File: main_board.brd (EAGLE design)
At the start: 100.3 x 69.8 mm, 46 parts, among them P1 ST-TF-003A, U1 STM32F407VGT6, U2 USBLC6-2, U3 MCP1700T-3302E, U4 LTC4054LES5-4.2#TRPBF, X1 MicroUSB-B

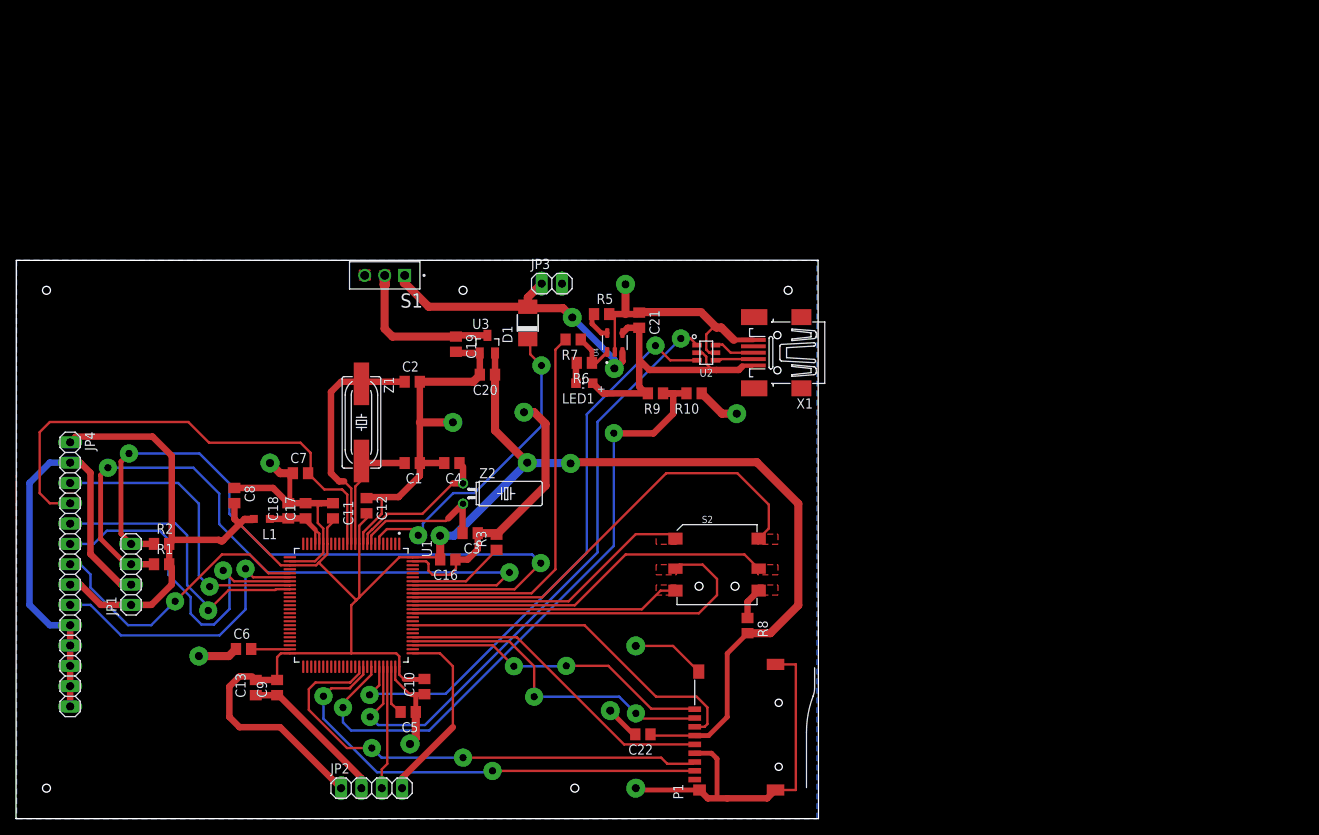
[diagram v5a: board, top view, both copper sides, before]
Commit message: updated pcb printouts
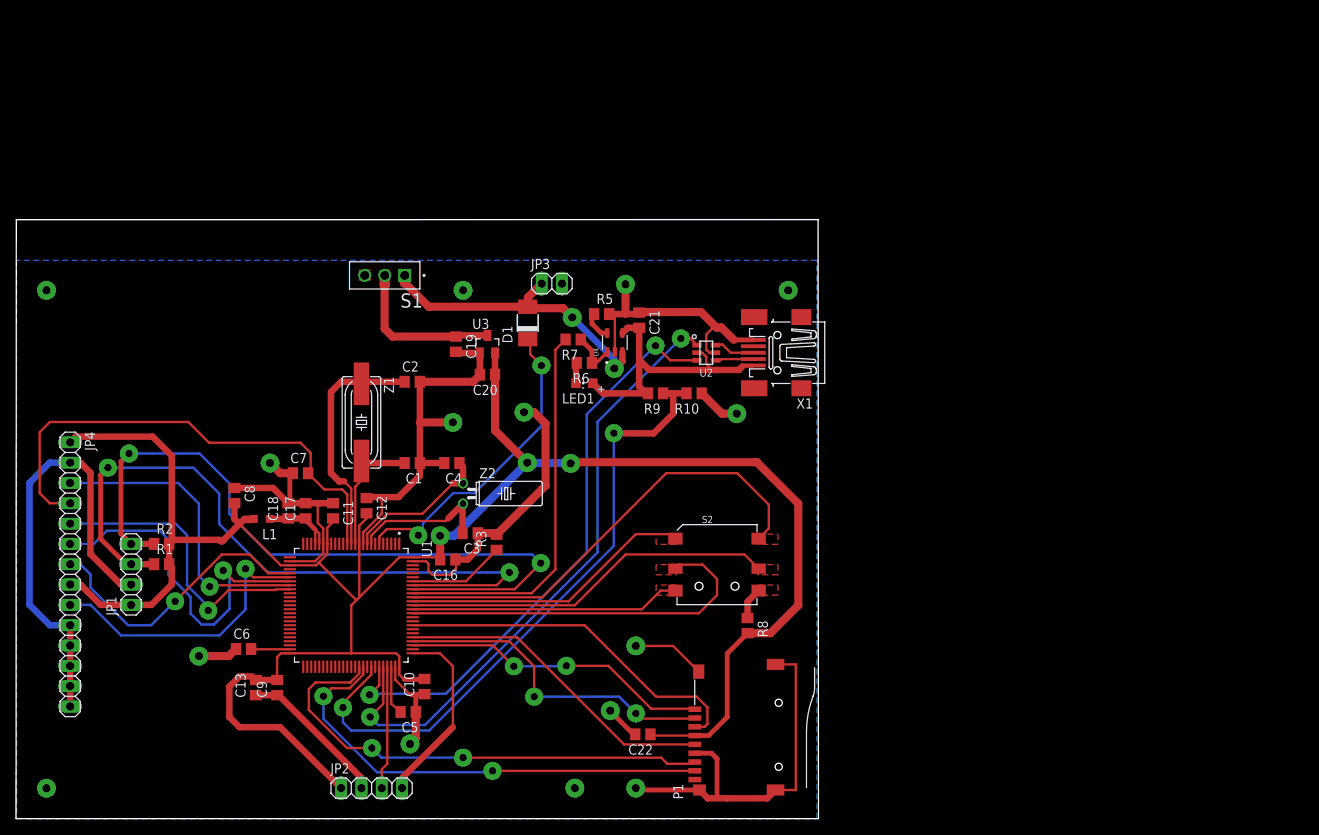
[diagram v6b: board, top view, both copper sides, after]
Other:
- board size 100.3 x 69.8 mm -> 100.3 x 74.9 mm
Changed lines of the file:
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@@
 <setting verticaltext="up"/>
 </settings>
-<grid distance="50" unitdist="mil" unit="mm" style="dots" multiple="1" display="yes" altdistance="5" altunitdist="mil" altunit="mm"/>
+<grid distance="50" unitdist="mil" unit="mm" style="dots" multiple="1" display="yes" altdistance="0.0127" altunitdist="mm" altunit="mm"/>
 <layers>
 <layer number="1" name="Top" color="4" fill="1" visible="yes" active="yes"/>
@@
 </layers>
 <board>
+<fusionsync huburn="a.YnVzaW5lc3M6cmFtYmxlcjY5Nw" projecturn="a.YnVzaW5lc3M6cmFtYmxlcjY5NyNEMjAxOTEyMjQyNDk2OTMxNTE" f3durn="urn:adsk.wipprod:dm.lineage:bHDcZ2FaTXqtTl9IB7PqNQ" pcbguid="" lastpulledtime="" lastsyncedchangeguid="" latestrevisionid="95c03de1-c068-4b4e-b2f2-ce3e2071d574" lastsyncedrevisionid="95c03de1-c068-4b4e-b2f2-ce3e2071d574" lastboardhashguid="d1d654ad-80bb-0683-6bda-78ac676d0201" lastpushedtime="2022-01-27T18:53:14Z" linktopcb3d="false"/>
 <plain>
 <wire x1="0" y1="0" x2="100.31" y2="0" width="0" layer="20" grouprefs="DISPLAY_BORDER"/>
-<wire x1="100.31" y1="0" x2="100.2592" y2="69.7994" width="0" layer="20"/>
-<wire x1="100.2592" y1="69.7994" x2="0.0381" y2="69.7867" width="0" layer="20"/>
-<wire x1="0.0381" y1="69.7867" x2="0" y2="0" width="0" layer="20" grouprefs="DISPLAY_BORDER"/>
+<wire x1="100.31" y1="0" x2="100.2592" y2="74.8794" width="0" layer="20"/>
+<wire x1="100.2592" y1="74.8794" x2="0.0381" y2="74.8667" width="0" layer="20"/>
+<wire x1="0.0381" y1="74.8667" x2="0" y2="0" width="0" layer="20" grouprefs="DISPLAY_BORDER"/>
 <wire x1="4.2291" y1="8.9408" x2="79.1591" y2="8.9408" width="0.3" layer="37" grouprefs="DISPLAY_BORDER"/>
 <wire x1="79.1591" y1="8.9408" x2="79.1591" y2="52.1208" width="0.3" layer="37" grouprefs="DISPLAY_BORDER"/>
 <wire x1="79.1591" y1="52.1208" x2="4.2291" y2="52.1208" width="0.3" layer="37" grouprefs="DISPLAY_BORDER"/>
 <wire x1="4.2291" y1="52.1208" x2="4.2291" y2="8.9408" width="0.3" layer="37" grouprefs="DISPLAY_BORDER"/>
-<hole x="3.81" y="66.04" drill="1"/>
-<hole x="3.81" y="3.81" drill="1"/>
-<hole x="96.52" y="66.04" drill="1"/>
-<hole x="69.85" y="3.81" drill="1"/>
-<hole x="55.88" y="66.04" drill="1"/>
 </plain>
 <attributes>
@@
 <contactref element="Z2" pad="1"/>
 <contactref element="C4" pad="1"/>
-<wire x1="43.91" y1="34.35" x2="43.9576" y2="34.3976" width="0.3" layer="1"/>
-<wire x1="43.9576" y1="34.3976" x2="43.9576" y2="35.59805" width="0.3" layer="1"/>
-<wire x1="43.9576" y1="35.59805" x2="44.49895" y2="36.1394" width="0.3" layer="1"/>
-<wire x1="44.51660625" y1="36.1394" x2="44.49895" y2="36.1394" width="0.3" layer="1"/>
-<wire x1="44.51660625" y1="36.1394" x2="46.47720625" y2="38.1" width="0.3" layer="1"/>
+<wire x1="43.91" y1="34.35" x2="43.9068" y2="34.3532" width="0.3" layer="1"/>
+<wire x1="43.9068" y1="35.59805" x2="43.9068" y2="34.3532" width="0.3" layer="1"/>
+<wire x1="43.9068" y1="35.59805" x2="46.40875" y2="38.1" width="0.3" layer="1"/>
 <wire x1="50.8" y1="38.1" x2="54.61" y2="41.91" width="0.3" layer="1"/>
 <wire x1="54.61" y1="41.91" x2="55.88" y2="41.91" width="0.8128" layer="1"/>
-<wire x1="46.47720625" y1="38.1" x2="50.8" y2="38.1" width="0.3" layer="1"/>
+<wire x1="46.40875" y1="38.1" x2="50.8" y2="38.1" width="0.3" layer="1"/>
 <wire x1="55.433" y1="44.45" x2="55.88" y2="44.003" width="0.3" layer="1"/>
 <wire x1="55.88" y1="44.003" x2="55.88" y2="41.91" width="0.8128" layer="1"/>
@@
 <wire x1="22.86" y1="30.353" x2="24.2062" y2="29.0068" width="0.3" layer="16"/>
 <via x="24.2062" y="29.0068" extent="1-16" drill="0.9"/>
-<wire x1="34.2154" y1="29.1719" x2="24.3713" y2="29.1719" width="0.3" layer="1"/>
+<wire x1="34.2281" y1="29.1719" x2="24.3713" y2="29.1719" width="0.3" layer="1"/>
 <wire x1="24.2062" y1="29.0068" x2="24.3713" y2="29.1719" width="0.3" layer="1"/>
-<wire x1="34.2173" y1="29.17" x2="34.2154" y2="29.1719" width="0.3" layer="1"/>
-<wire x1="34.2173" y1="29.17" x2="34.23" y2="29.17" width="0.3" layer="1"/>
+<wire x1="34.23" y1="29.17" x2="34.2281" y2="29.1719" width="0.3" layer="1"/>
 </signal>
 <signal name="LCD_DC">
@@
 <via x="24.0284" y="26.0223" extent="1-16" drill="0.9"/>
 <wire x1="24.0284" y1="26.0223" x2="26.5811" y2="28.575" width="0.3" layer="1"/>
-<wire x1="32.385" y1="28.575" x2="32.4866" y2="28.6766" width="0.3" layer="1"/>
-<wire x1="32.4866" y1="28.6766" x2="34.2234" y2="28.6766" width="0.3" layer="1"/>
-<wire x1="34.2234" y1="28.6766" x2="34.23" y2="28.67" width="0.3" layer="1"/>
+<wire x1="32.385" y1="28.575" x2="32.4739" y2="28.6639" width="0.3" layer="1"/>
+<wire x1="34.23" y1="28.67" x2="34.2239" y2="28.6639" width="0.3" layer="1"/>
+<wire x1="34.2239" y1="28.6639" x2="32.4739" y2="28.6639" width="0.3" layer="1"/>
 <wire x1="19.939" y1="36.8808" x2="21.3868" y2="35.433" width="0.3" layer="16"/>
 <wire x1="26.5811" y1="28.575" x2="32.385" y2="28.575" width="0.3" layer="1"/>
@@
 </polygon>
 </signal>
+<signal name="N$4">
+<via x="3.81" y="66.04" extent="1-16" drill="1"/>
+</signal>
+<signal name="N$12">
+<via x="55.88" y="66.04" extent="1-16" drill="1"/>
+</signal>
+<signal name="N$13">
+<via x="96.52" y="66.04" extent="1-16" drill="1"/>
+</signal>
+<signal name="N$14">
+<via x="3.81" y="3.81" extent="1-16" drill="1"/>
+</signal>
+<signal name="N$15">
+<via x="69.85" y="3.81" extent="1-16" drill="1"/>
+</signal>
 </signals>
 <mfgpreviewcolors>
@@
 </note>
 <note version="8.3" severity="warning">
+Since Version 8.3, EAGLE supports Fusion synchronisation.
+This feature will not be available in this version and saving
+the document will break the link to the Fusion PCB feature.
+</note>
+<note version="8.3" severity="warning">
